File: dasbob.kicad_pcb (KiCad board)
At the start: 2 copper layers, 243.5 x 104.8 mm, 68 parts, among them J1 TRRS LEFT, J2 TRRS LEFT, SW1 SW_Push, SW10 SW_Push, SW11 SW_Push, SW12 SW_Push, SW13 SW_Push, SW14 SW_Push, SW15 SW_Push, SW16 SW_Push, SW17 SW_Push, SW18 SW_Push, SW19 SW_Push, SW2 SW_Push, SW20 SW_Push, SW21 SW_Push, SW22 SW_Push, SW23 SW_Push, SW24 SW_Push, SW25 SW_Push, SW26 SW_Push, SW27 SW_Push, SW28 SW_Push, SW29 SW_Push, SW3 SW_Push, SW30 SW_Push, SW31 SW_Push, SW32 SW_Push, SW33 SW_Push, SW34 SW_Push, SW35 SW_Push, SW36 SW_Push, SW4 SW_Push, SW5 SW_Push, SW6 SW_Push, SW7 SW_Push, SW8 SW_Push, SW9 SW_Push, U1 Elite-C RIGHT, U2 Elite-C LEFT, U3 OLED1, U4 OLED2

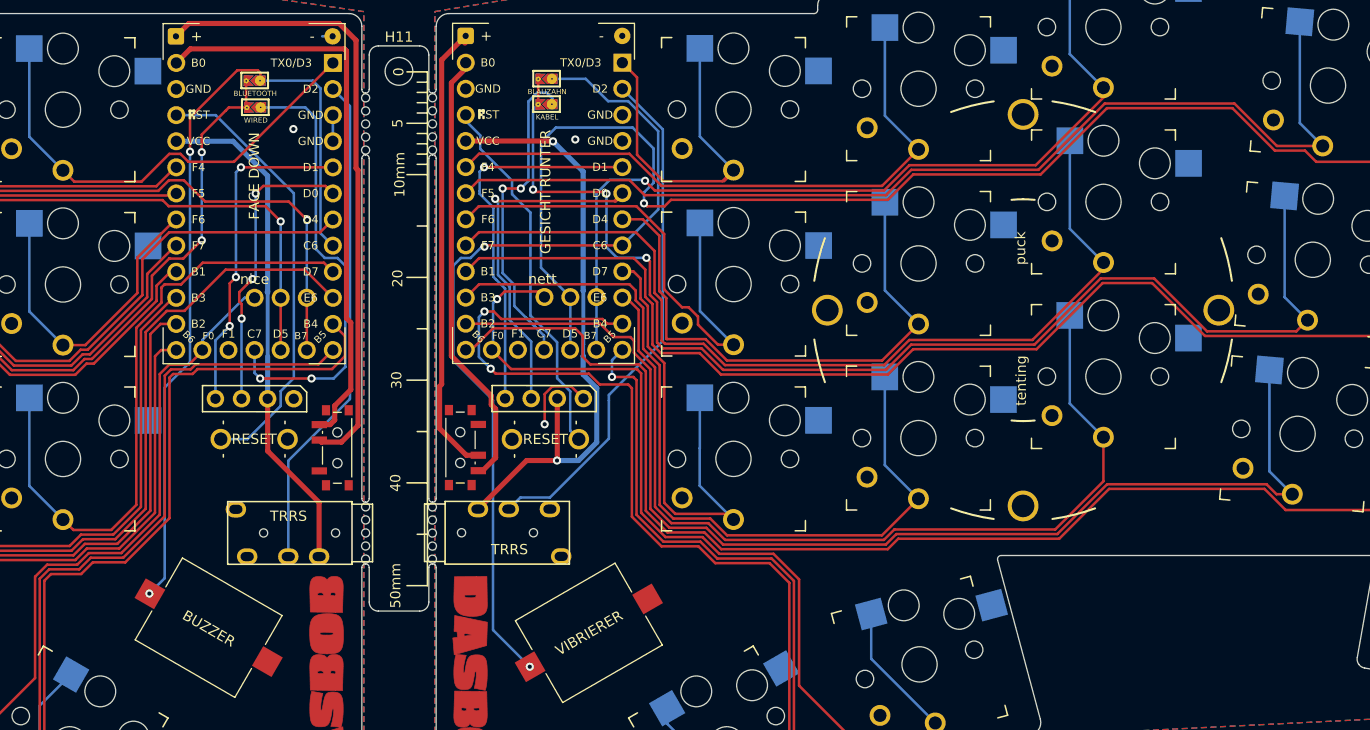
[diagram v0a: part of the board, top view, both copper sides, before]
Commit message: Remove jumpers
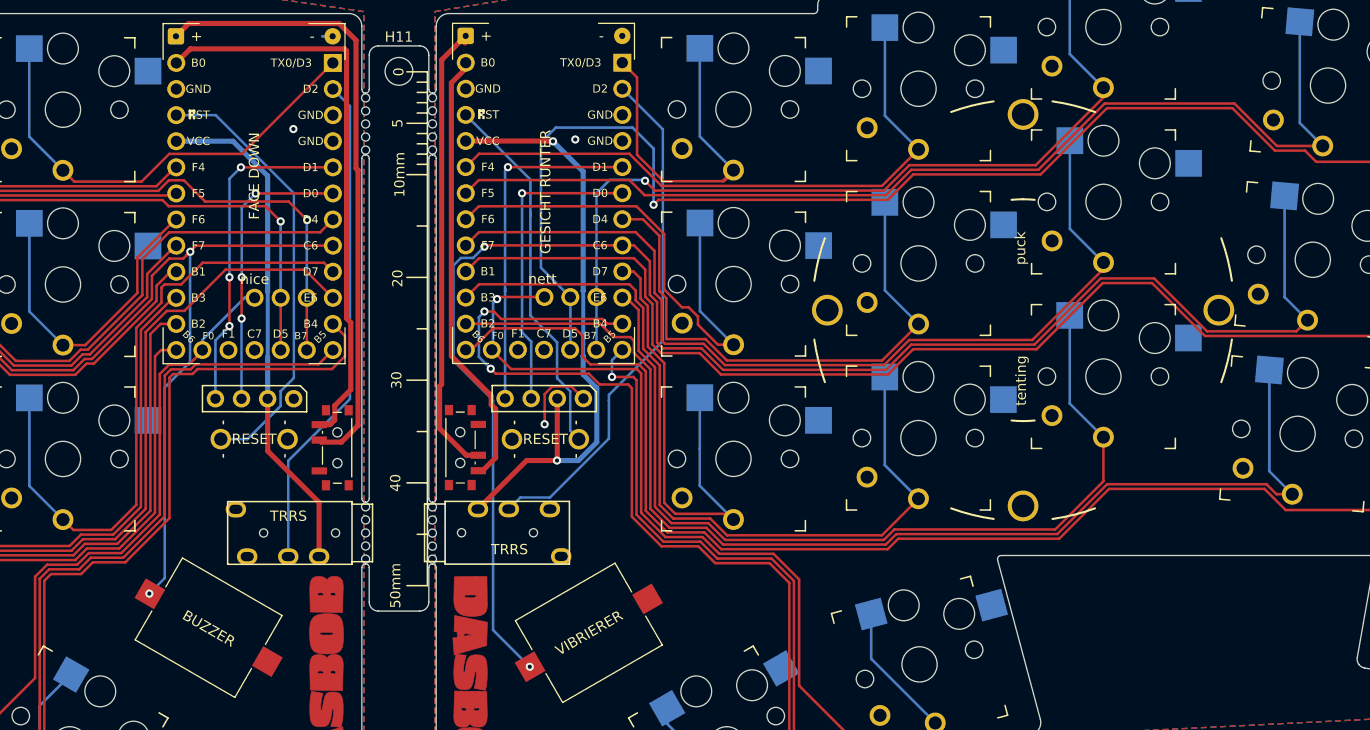
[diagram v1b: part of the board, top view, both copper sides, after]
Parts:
- removed JP1: BLUETOOTH, keebio:JUMPER_SMD_2DUB
- removed JP2: WIRED, keebio:JUMPER_SMD_2DUB
- removed JP3: BLAUZAHN, keebio:JUMPER_SMD_2DUB
- removed JP4: KABEL, keebio:JUMPER_SMD_2DUB
- RST1: value SW_Push -> RESET BUTTON RIGHT
- TSR1: value SW_Push -> RESET BUTTON LEFT
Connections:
- BZ1 pad 1: SOUND -> 7
- BZ2 pad 1: DNUOS -> 7a
- U1 pad 27: C7 -> unconnected-(U1-C7-Pad27)
- U1 pad 8: SOUND -> 7
- U2 pad 27: C7a -> unconnected-(U2-C7-Pad27)
- U2 pad 8: DNUOS -> 7a
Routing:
- net DNUOS: track 84.4 -> 0.00 mm, vias 2 -> 0
- net SOUND: track 79.6 -> 0.00 mm, vias 2 -> 0
- net C7: track 43.6 -> 0.00 mm, vias 2 -> 0
- net 7a: track 120.3 -> 154.8 mm, vias 3 -> 2
- net C7a: track 33.2 -> 0.00 mm, vias 2 -> 0
- net 7: track 113.0 -> 142.6 mm
- net 2P: track 34.8 -> 30.3 mm
- net 1P: track 37.2 -> 34.0 mm
- net GND: track 3.56 -> 1.02 mm
- net 1a: track 149.2 -> 147.8 mm
- net TSR: track 35.5 -> 36.4 mm
- net P2: track 28.9 -> 28.1 mm
- net 5: track 45.4 -> 44.7 mm

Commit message: some tweaks
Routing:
- net CVV: track 59.9 -> 61.9 mm
- net DNG: track 7.50 -> 9.45 mm
- net 2P: track 30.3 -> 28.3 mm
- net 1P: track 34.0 -> 33.1 mm
